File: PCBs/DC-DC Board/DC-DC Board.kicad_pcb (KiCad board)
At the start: 2 copper layers, 58.4 x 36.8 mm, 7 parts, among them J1 Conn_01x01, J2 Conn_01x01, J3 Conn_01x01, J4 Conn_01x01, U1 MurataDC-DC, U2 ACS711

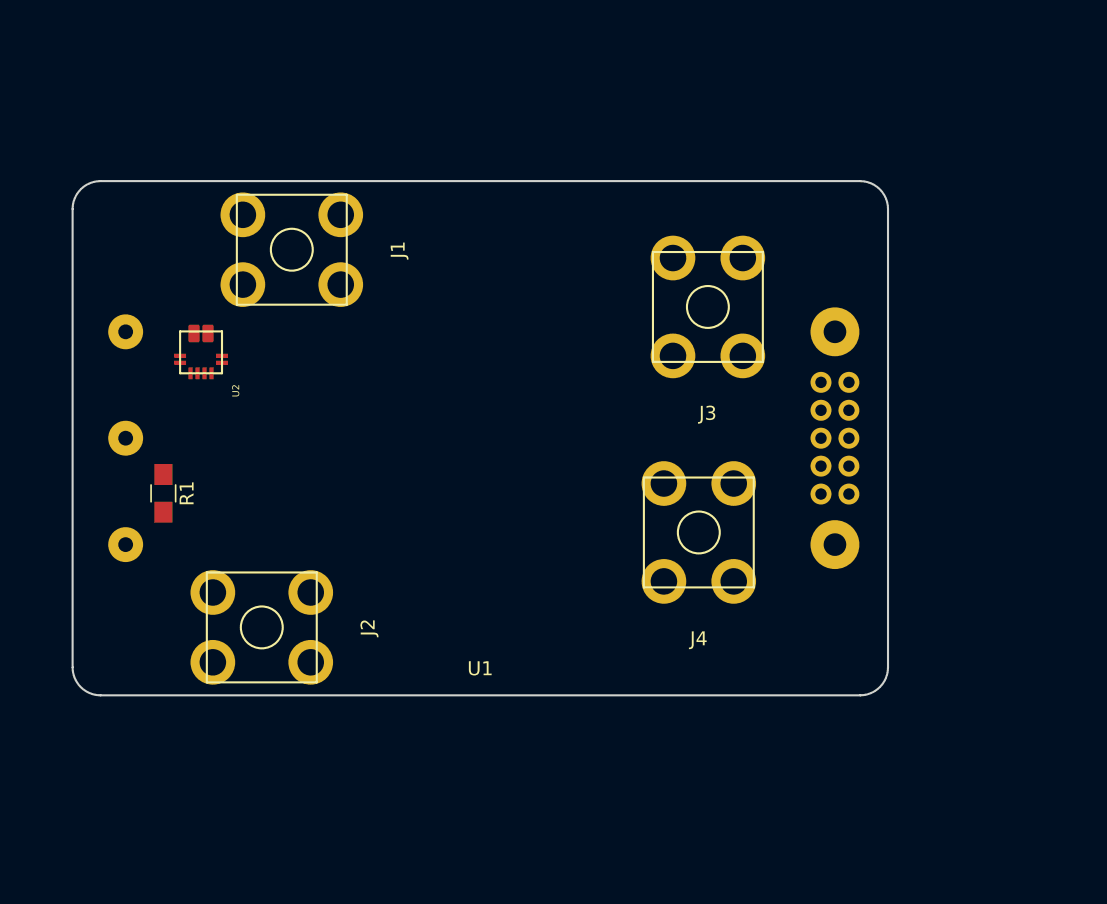
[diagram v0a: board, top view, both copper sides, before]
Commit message: Semi Final DC-DC Schematic
Pretty much finalized the schematic and component selection for the no-micro version of the DC-DC board. The micro version will come later.
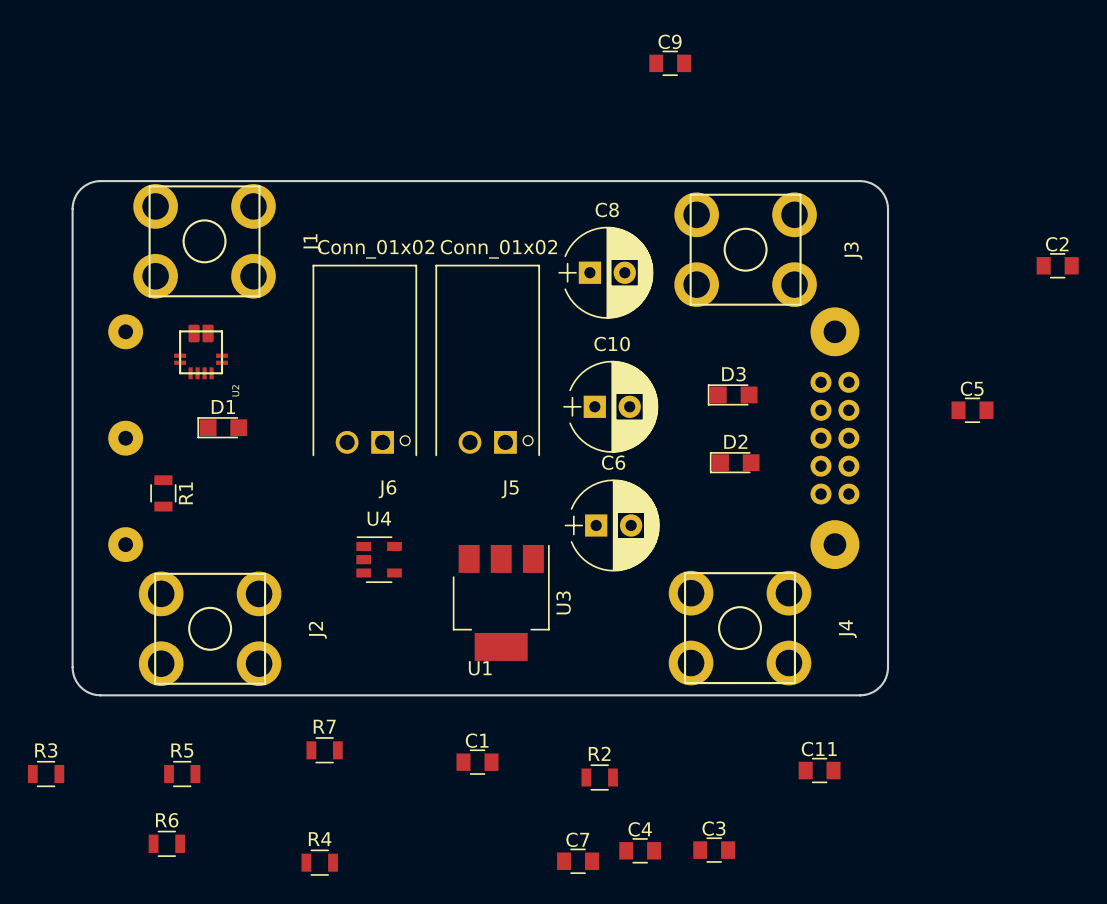
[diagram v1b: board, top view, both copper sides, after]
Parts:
- added C1: 1uF, Capacitors_SMD:C_0805, F.Cu at (99.8, 73.2)
- added C10: 220uF, Capacitors_THT:CP_Radial_D6.3mm_P2.50mm, F.Cu at (108.2, 47.8)
- added C11: 1uF, Capacitors_SMD:C_0805, F.Cu at (124.3, 73.8)
- added C2: 0.1uF, Capacitors_SMD:C_0805, F.Cu at (141.3, 37.6)
- added C3: 4.7nF, Capacitors_SMD:C_0805, F.Cu at (116.8, 79.5)
- added C4: 4.7nF, Capacitors_SMD:C_0805, F.Cu at (111.5, 79.5)
- added C5: 1uF, Capacitors_SMD:C_0805, F.Cu at (135.2, 48.0)
- added C6: 47uF, Capacitors_THT:CP_Radial_D6.3mm_P2.50mm, F.Cu at (108.3, 56.2)
- added C7: 1uF, Capacitors_SMD:C_0805, F.Cu at (107.0, 80.3)
- added C8: 220uF, Capacitors_THT:CP_Radial_D6.3mm_P2.50mm, F.Cu at (107.8, 38.1)
- added C9: 1uF, Capacitors_SMD:C_0805, F.Cu at (113.6, 23.1)
- added D1: LED, LEDs:LED_0805, F.Cu at (81.6, 49.2)
- added D2: LED, LEDs:LED_0805, F.Cu at (118.3, 51.8)
- added D3: LED, LEDs:LED_0805, F.Cu at (118.2, 46.9)
- added J5: Conn_01x02, EER:MOLEX_0705530001, F.Cu at (101.8, 50.3)
- added J6: Conn_01x02, EER:MOLEX_0705530001, F.Cu at (93.0, 50.3)
- added R2: 10k, Resistors_SMD:R_0805, F.Cu at (108.5, 74.3)
- added R3: 0, Resistors_SMD:R_0805, F.Cu at (68.9, 74.0)
- added R4: 0, Resistors_SMD:R_0805, F.Cu at (88.5, 80.4)
- added R5: 1k, Resistors_SMD:R_0805, F.Cu at (78.7, 74.0)
- added R6: 880, Resistors_SMD:R_0805, F.Cu at (77.5, 79.0)
- added R7: 0, Resistors_SMD:R_0805, F.Cu at (88.8, 72.3)
- added U3: MC33375, TO_SOT_Packages_SMD:SOT-223, F.Cu at (101.5, 61.8)
- added U4: TLV733P, TO_SOT_Packages_SMD:SOT-23-5, F.Cu at (92.8, 58.7)
- R1: footprint Resistors_SMD:R_0805_HandSoldering -> Resistors_SMD:R_0805
- moved J4 7.46 mm to (118.6, 63.6), turned to 90 degrees
- moved J1 6.28 mm to (80.2, 35.9)
- moved J3 4.91 mm to (119.0, 36.5), turned to 90 degrees
- moved J2 3.70 mm to (80.7, 63.6)
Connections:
- net Net-(U1-Pad14) renamed SMBALERT
- U1 pad 10: Net-(U1-Pad10) -> SCL
- U1 pad 11: Net-(U1-Pad11) -> SDA
- U1 pad 12: Net-(U1-Pad12) -> PG
- U1 pad 13: Net-(U1-Pad13) -> GND
- U1 pad 6: Net-(U1-Pad6) -> +12V
- U1 pad 7: Net-(U1-Pad7) -> GND
- U2 pad 11: Net-(U2-Pad11) -> VIOUT
- U2 pad 12: Net-(U2-Pad12) -> +3V3

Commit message: DC-DC Board Final
99% Done the first DC-DC Board. Just need to double check everything!!
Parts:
- removed R7: 0, Resistors_SMD:R_0805
- added C12: 1uF, Capacitors_SMD:C_0805, F.Cu at (87.0, 57.0)
- added C13: 0.1uF, Capacitors_SMD:C_0805, F.Cu at (87.0, 55.0)
- added R8: 1k, Resistors_SMD:R_0805, F.Cu at (79.7, 48.9)
- added TP1: TestPoint, Testpoints:TestPoint_Pad_D1.0mm, F.Cu at (85.0, 45.6)
- added TP2: TestPoint, Testpoints:TestPoint_Pad_D1.0mm, F.Cu at (92.8, 56.9)
- added U$12: EERLOGO, EER:EERLOGO, B.Cu at (106.1, 43.9)
- added U$15: MUNLOGO, EER:MUNLOGO, B.Cu at (107.3, 68.4)
- J5: value Conn_01x02 -> PMBus
- J6: value Conn_01x02 -> Current Sense
- R6: value 880 -> 1k
- U3: value MC33375 -> NCP551; footprint TO_SOT_Packages_SMD:SOT-223 -> TO_SOT_Packages_SMD:SOT-23-5
- moved C2 58.9 mm to (83.7, 49.5), turned to 270 degrees
- moved R6 52.4 mm to (121.2, 50.1)
- moved R3 52.1 mm to (117.4, 55.0), turned to 270 degrees
- moved R5 49.9 mm to (121.2, 48.0)
- moved R2 43.2 mm to (74.6, 47.5), turned to 180 degrees
- moved R4 40.1 mm to (119.5, 55.0), turned to 270 degrees
- moved C9 39.0 mm to (96.0, 57.9), turned to 90 degrees
- moved C11 38.6 mm to (88.2, 60.0), turned to 90 degrees
- moved C5 34.7 mm to (103.5, 62.0), turned to 270 degrees
- moved C1 27.6 mm to (85.6, 49.5), turned to 270 degrees
- moved C4 26.7 mm to (121.7, 54.9), turned to 270 degrees
- moved C3 24.5 mm to (115.2, 55.0), turned to 270 degrees
- moved C7 21.3 mm to (96.0, 62.1), turned to 270 degrees
- moved D1 7.87 mm to (74.7, 45.5), turned to 180 degrees
- moved D2 6.86 mm to (118.6, 44.9), turned to 90 degrees
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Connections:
- U1 pad 15: Net-(R7-Pad1) -> GND
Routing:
- net GND: track 0.00 -> 34.3 mm, vias 0 -> 10
- net SDA: track 0.00 -> 33.6 mm, vias 0 -> 1
- net SCL: track 0.00 -> 27.8 mm
- net +3V3: track 0.00 -> 25.6 mm, vias 0 -> 2
- net +12V: track 0.00 -> 19.7 mm, vias 0 -> 1
- net Net-(C3-Pad1): track 0.00 -> 16.7 mm
- net VIOUT: track 0.00 -> 16.6 mm
- net Earth: track 0.00 -> 15.1 mm
- net /+48V: track 0.00 -> 10.8 mm
- net Net-(D3-Pad1): track 0.00 -> 6.99 mm
- net Net-(C4-Pad1): track 0.00 -> 6.17 mm
- net Net-(R8-Pad2): track 0.00 -> 4.75 mm
- net Net-(D2-Pad1): track 0.00 -> 3.03 mm
- net Net-(R1-Pad1): track 0.00 -> 2.80 mm
- net PG: track 0.00 -> 2.20 mm
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- added copper zone on B.Cu, net +12V
- added copper zone on F.Cu, net +12V
- added copper zone on F.Cu, net +3V3
- added copper zone on B.Cu, net /+48V
- added copper zone on F.Cu, net /+48V
- added copper zone on F.Cu, net /5V
- added copper zone on B.Cu, net Earth
- added copper zone on F.Cu, net Earth
- added copper zone on B.Cu, net GND
- added copper zone on F.Cu, net GND
- added copper zone on F.Cu, net Net-(U1-Pad1)
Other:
- board text added: "+12V"
- board text added: "+48V"
- board text added: "DC-DC Board - No Micro"
- board text added: "Eastern Edge Robotics"
- board text added: "FAULT"
- board text added: "Mark Belbin - 2018"

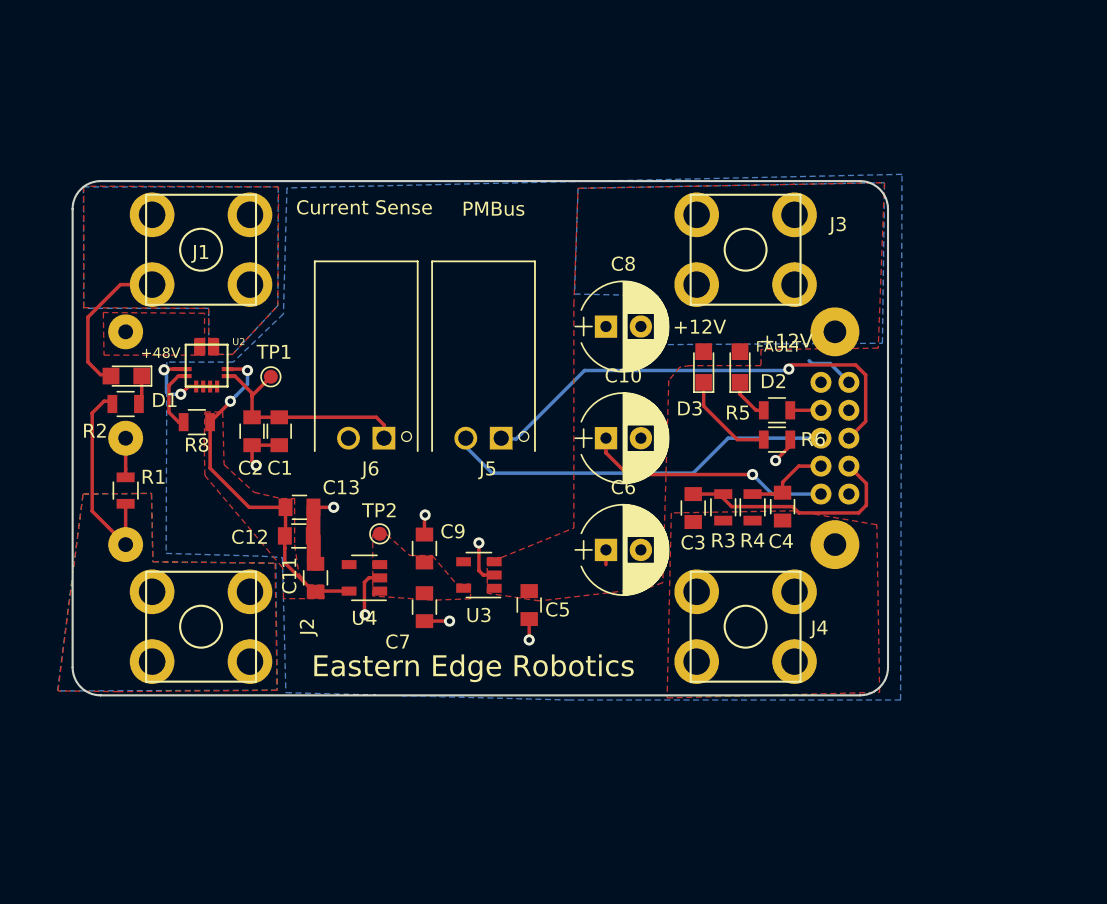
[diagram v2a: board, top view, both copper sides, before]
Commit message: DC-DC Touchups
Silk screen mostly
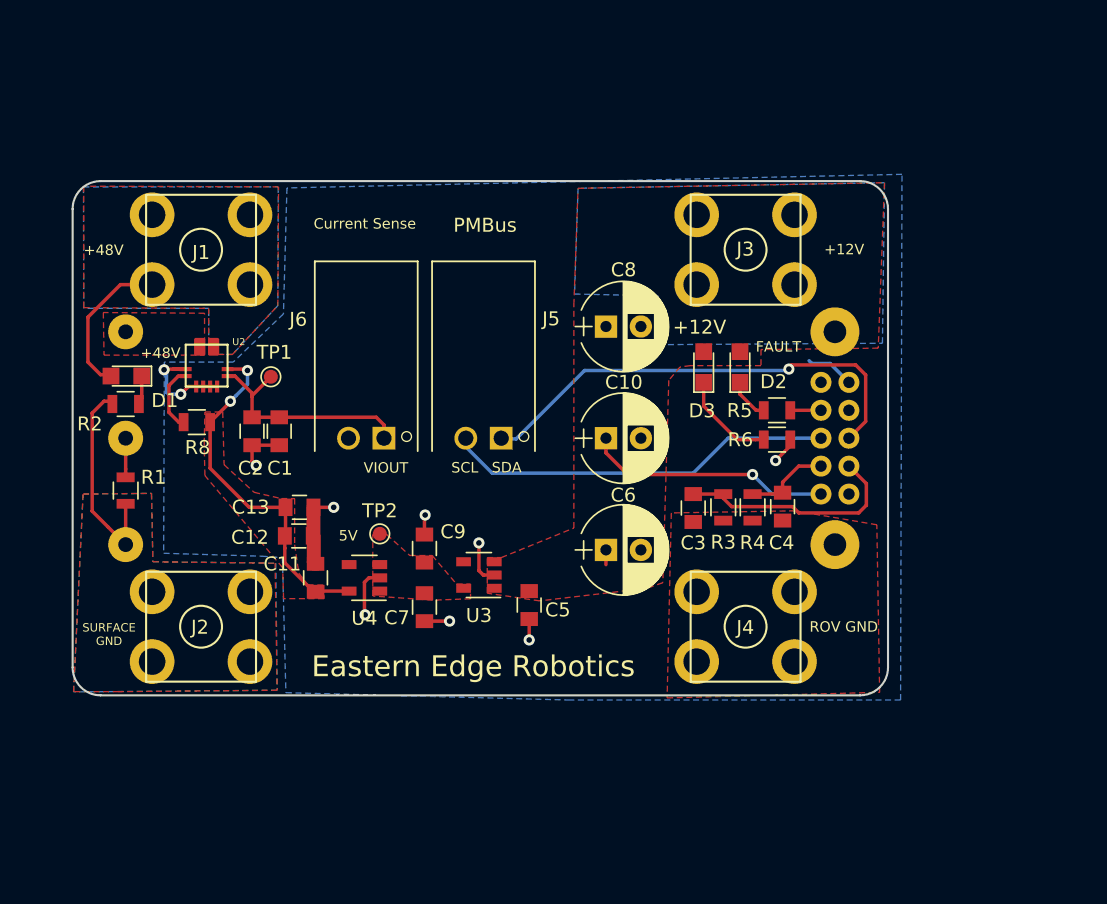
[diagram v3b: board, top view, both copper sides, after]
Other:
- board text added: "5V"
- board text added: "ROV GND"
- board text added: "SCL"
- board text added: "SDA"
- board text added: "SURFACE GND"
- board text added: "VIOUT"

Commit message: Fixed DC-DC
After looking at the IRL DC-DCs, I realized I had the footprint mirrored (the datasheet is not intuitive). I rerouted pretty much everything to fix it. RIP
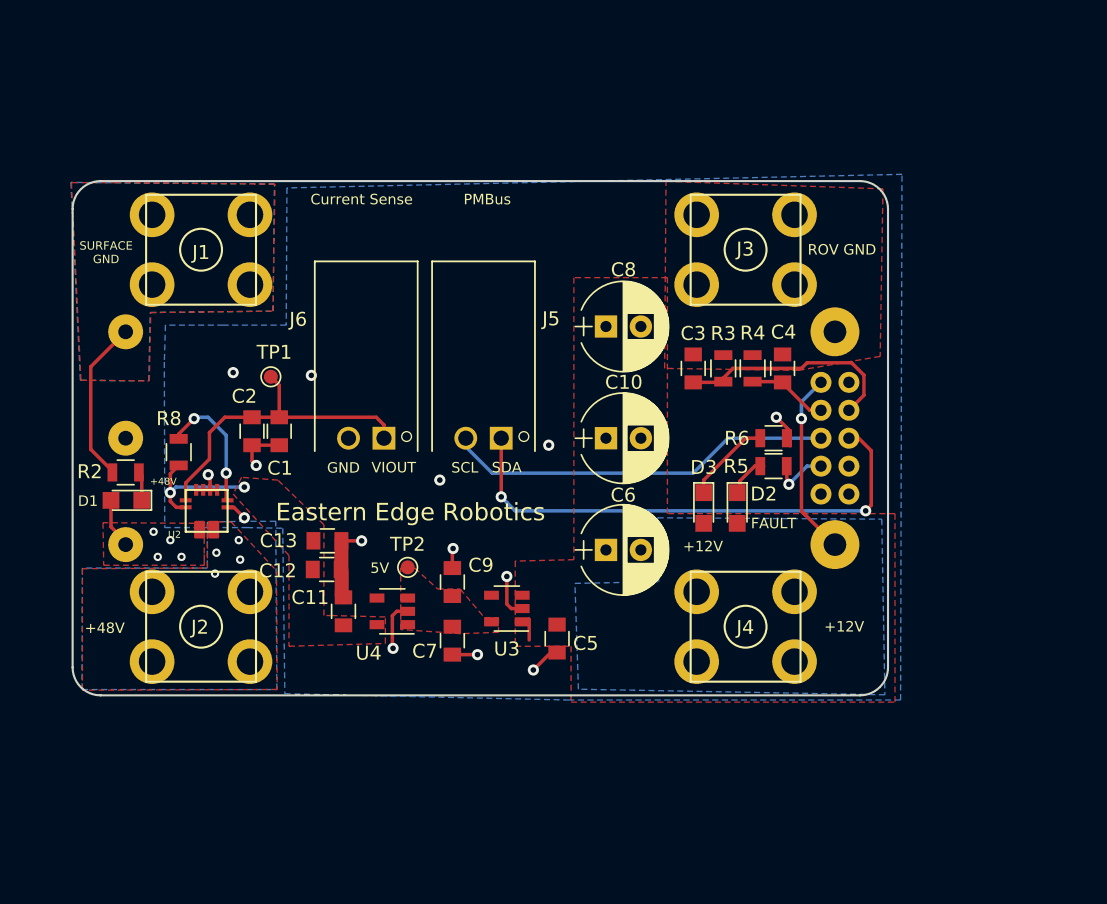
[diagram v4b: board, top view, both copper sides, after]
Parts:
- removed R1: 0, Resistors_SMD:R_0805
- added U$16: MILOGO, EER:MILOGO, B.Cu at (106.8, 56.3)
- J5: value PMBus -> Conn_01x02
- J6: value Current Sense -> Conn_01x02
- moved U2 10.4 mm to (80.4, 55.2), turned to 90 degrees
- moved D2 10.1 mm to (118.4, 55.0), turned to 270 degrees
- moved D3 10.1 mm to (116.0, 55.0), turned to 270 degrees
- moved C3 10.0 mm to (115.2, 45.0), turned to 90 degrees
- moved R3 9.95 mm to (117.4, 45.0), turned to 90 degrees
- moved R4 9.95 mm to (119.5, 45.0), turned to 90 degrees
- moved C4 9.90 mm to (121.7, 45.0), turned to 90 degrees
- moved D1 8.90 mm to (74.7, 54.5)
- moved R2 4.90 mm to (74.6, 52.5)
- moved R5 4.01 mm to (121.0, 52.0)
- moved U3 3.12 mm to (101.9, 62.2)
- moved C11 3.12 mm to (90.2, 62.4)
- moved C12 3.12 mm to (89.0, 59.4)
- moved C13 3.12 mm to (89.0, 57.4)
- moved C7 3.12 mm to (98.0, 64.5)
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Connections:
- D1 pad 2: /+48V -> Net-(D1-Pad2)
- J1 pad 1: /+48V -> Earth
- J2 pad 1: Earth -> /+48V
- J3 pad 1: +12V -> GND
- J4 pad 1: GND -> +12V
- U1 pad 1: Net-(U1-Pad1) -> Net-(D1-Pad2)
- U2 pad 1: /+48V -> Net-(D1-Pad2)
- U2 pad 3: Net-(U1-Pad1) -> /+48V
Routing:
- net +3V3: track 25.6 -> 9.83 mm
- net /+48V: track 10.8 -> 0.00 mm, vias 0 -> 4
- net VIOUT: track 16.6 -> 22.8 mm
- net GND: track 34.3 -> 28.6 mm, vias 10 -> 14
- net Net-(R8-Pad2): track 4.75 -> 9.75 mm, vias 0 -> 2
- net +12V: track 19.7 -> 15.5 mm
- net Net-(D1-Pad2): track 0.00 -> 3.60 mm, vias 0 -> 4
- net SDA: track 33.6 -> 37.2 mm, vias 1 -> 2
- net Earth: track 15.1 -> 11.7 mm
- net Net-(U1-Pad2): track 2.80 -> 0.00 mm
- net PG: track 2.20 -> 4.20 mm, vias 0 -> 1
- net Net-(D3-Pad1): track 6.99 -> 6.44 mm
- added copper zone on F.Cu, net Net-(D1-Pad2)
- removed copper zone on F.Cu, net Net-(U1-Pad1)
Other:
- rule trace_min: 0.2 -> 0.25
- rule via_min_size: 0.4 -> 0.3
- board text added: "Current Sense"
- board text added: "GND"
- board text added: "PMBus"

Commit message: Added Reverse Polarity Protection
Accomplished with an NMOS on the primary on/off pin. Still need to verify this is OK in the lab.
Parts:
- added Q1: Q_NMOS_DGS, EER:SOT-23-NMOS, F.Cu at (75.8, 46.9)
- added R1: 700k, Resistors_SMD:R_0603, F.Cu at (72.2, 54.1)
- added R7: 100k, Resistors_SMD:R_0603, F.Cu at (72.2, 47.6)
- moved R2 0.73 mm to (75.3, 52.6)
- moved D1 0.49 mm to (75.1, 54.6)
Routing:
- net Net-(Q1-Pad2): track 0.00 -> 10.9 mm
- net Earth: track 11.7 -> 20.9 mm, vias 0 -> 1
- net Net-(Q1-Pad1): track 0.00 -> 2.63 mm
- net Net-(D1-Pad2): track 3.60 -> 5.49 mm

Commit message: DC-DC Board DONE
Should be done for sure now bys
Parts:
- removed D2: LED, LEDs:LED_0805
- removed R5: 1k, Resistors_SMD:R_0805
- removed TP1: TestPoint, Testpoints:TestPoint_Pad_D1.0mm
- added R9: 0, Resistors_SMD:R_0603, F.Cu at (75.7, 47.4)
- Q1: value Q_NMOS_DGS -> Q_NMOS_GDS; footprint EER:SOT-23-NMOS -> TO_SOT_Packages_SMD:TO-252-2
- R7: value 100k -> 200k
- moved Q1 6.67 mm to (82.0, 44.4), turned to 0 degrees
- moved D3 4.08 mm to (120.1, 54.8)
- moved C1 1.91 mm to (87.0, 50.8)
- moved C2 1.84 mm to (85.0, 50.8)
- moved J5 0.62 mm to (102.1, 50.0)
- moved J6 0.47 mm to (93.6, 50.0)
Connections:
- net SMBALERT renamed Net-(U1-Pad14)
- J1 pad 1: Earth -> Net-(J1-Pad1)
- Q1 pad 2: Net-(Q1-Pad2) -> Net-(J1-Pad1)
- R1 pad 2: Net-(Q1-Pad2) -> Net-(Q1-Pad1)
- R7 pad 1: Net-(Q1-Pad2) -> Net-(Q1-Pad1)
- U1 pad 12: PG -> Net-(U1-Pad12)
- U1 pad 2: Net-(Q1-Pad1) -> Net-(R9-Pad1)
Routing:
- net Net-(Q1-Pad1): track 2.63 -> 20.4 mm, vias 0 -> 2
- net Net-(Q1-Pad2): track 10.9 -> 0.00 mm
- net Earth: track 20.9 -> 12.2 mm, vias 1 -> 9
- net VIOUT: track 22.8 -> 18.4 mm
- net PG: track 4.20 -> 0.00 mm, vias 1 -> 0
- net Net-(D2-Pad1): track 2.98 -> 0.00 mm
- net Net-(D3-Pad1): track 6.44 -> 3.83 mm
- net Net-(R9-Pad1): track 0.00 -> 2.50 mm
- net Net-(R8-Pad2): track 9.75 -> 7.73 mm
- net GND: track 28.6 -> 30.4 mm, vias 14 -> 30
- net Net-(J1-Pad1): vias 0 -> 27
- net /+48V: vias 4 -> 17
- net +12V: vias 1 -> 28
- added copper zone on B.Cu, net Net-(D1-Pad2)
- added copper zone on B.Cu, net Net-(J1-Pad1)
- added copper zone on F.Cu, net Net-(J1-Pad1)
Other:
- board text removed: "FAULT"
